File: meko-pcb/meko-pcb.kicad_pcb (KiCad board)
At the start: 4 copper layers, 37 x 69 mm, 213 parts, among them IC2 TPS7A2033PDBVR, IC4 TAD5212IRGER, IC5 AS5600-ASOM, J1 USB_C_Receptacle_USB2.0_16P, J3 GDEY0154D67, J4 Conn_ARM_SWD_TagConnect_TC203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, J5 503398-1892, Q1 SS8050, Q2 Si1308EDL, SW1 SW_Push, SW2 SW_Push, SW3 SW_Push, SW4 SW_Push, SW5 SW_Push, SW6 SW_Push, SW7 SW_Push, SW9 SW_Push, U2 nRF5340-QKxx, U3 nPM1300-CAXX, Y1 32MHz, Y2 32.768 kHz

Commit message: started layout
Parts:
- removed U3: nPM1300-CAXX, PCM_nordic-lib-kicad-npm:BGA-35_7x5_3.077x2.3775mm
- added U1: nPM1300-QEXX, Package_DFN_QFN:QFN-32-1EP_5x5mm_P0.5mm_EP3.6x3.6mm_ThermalVias, B.Cu at (104.0, 78.5)
- AE1, C13, C18, C31, C32, C7, C8, D1, D10, D12, D14, D6, D7, D8, D9, JP4, L1, L2, L5, U2, Y1, Y2: moved to B.Cu
- R10, R11, R12, R13, R14, R15, R16, R17, R18, R19, R2, R3, R4, R5, R6, R7, R8, R9: footprint Resistor_SMD:R_0402_1005Metric -> Resistor_SMD:R_0603_1608Metric
- moved C13 80.6 mm to (108.7, 61.1), turned to 180 degrees
- moved C18 79.7 mm to (107.0, 64.6), turned to 90 degrees
- moved C7 79.4 mm to (103.0, 66.8), turned to 180 degrees
- moved C8 77.1 mm to (100.7, 69.5), turned to 90 degrees
- moved C53 76.1 mm to (106.4, 54.4), turned to -90 degrees
- moved C54 72.9 mm to (99.6, 50.2), turned to -90 degrees
- moved D14 72.5 mm to (89.4, 16.1), turned to 90 degrees
- moved D12 71.8 mm to (92.4, 16.1), turned to 90 degrees
- moved C51 71.6 mm to (104.6, 57.6), turned to 90 degrees
- moved D6 71.6 mm to (104.2, 16.1), turned to 90 degrees
- moved D10 71.4 mm to (95.3, 16.1), turned to 90 degrees
- moved D7 71.3 mm to (101.2, 16.1), turned to 90 degrees
- moved D9 71.2 mm to (98.3, 16.1), turned to 90 degrees
- moved C63 66.5 mm to (104.6, 54.5), turned to -90 degrees
- moved C49 63.2 mm to (96.0, 53.2)
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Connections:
- net Net-(U2-AIN6/P0.27) renamed /PMIC_GPIO4
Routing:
- net /DISPL_VCOM: track 0.00 -> 4.10 mm

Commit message: almost finished with general layout
this will most certanily evolve
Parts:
- added C39: 1uF, Capacitor_SMD:C_0603_1608Metric, F.Cu at (100.5, 71.4)
- added TP7: DISPL_SDA, TestPoint:TestPoint_Pad_D1.0mm, F.Cu at (120.1, 71.9)
- C1, C11, C12, C17, C19, C2, C22, C30, C35, C37, C42, C44, L3, R10, R12, R6, R9: moved to B.Cu
- D8: moved to F.Cu
- L1: value 10uH -> 2.2nH; footprint Inductor_SMD:L_1008_2520Metric -> Inductor_SMD:L_0603_1608Metric
- moved C35 83.1 mm to (99.3, 37.3), turned to 180 degrees
- moved C22 78.2 mm to (104.5, 69.5)
- moved C34 77.5 mm to (94.3, 37.5)
- moved C15 76.3 mm to (104.3, 64.7)
- moved C30 75.9 mm to (94.7, 33.1)
- moved C1 75.7 mm to (99.8, 60.8), turned to 90 degrees
- moved C12 73.7 mm to (100.2, 76.7), turned to -90 degrees
- moved C24 72.2 mm to (104.3, 66.3)
- moved C2 72.0 mm to (96.2, 60.8), turned to 90 degrees
- moved C11 70.6 mm to (93.8, 74.6), turned to -90 degrees
- moved C17 70.4 mm to (98.5, 76.7), turned to -90 degrees
- moved C5 70.3 mm to (94.3, 75.2), turned to 180 degrees
- moved C9 70.2 mm to (94.3, 76.9), turned to 180 degrees
- moved C14 69.9 mm to (97.5, 75.2)
- moved C20 69.5 mm to (97.5, 76.9)
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
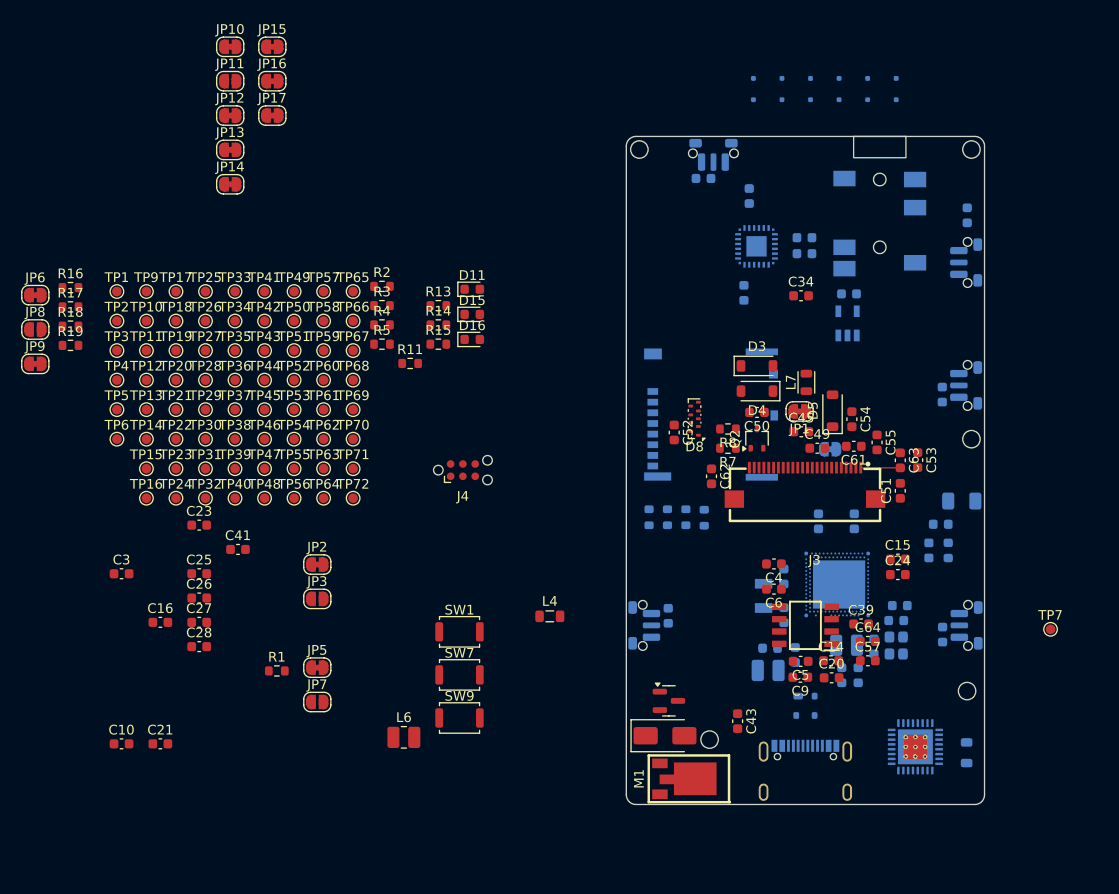
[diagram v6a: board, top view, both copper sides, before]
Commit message: finished first pass of rough layout
i still need to add 3d modles
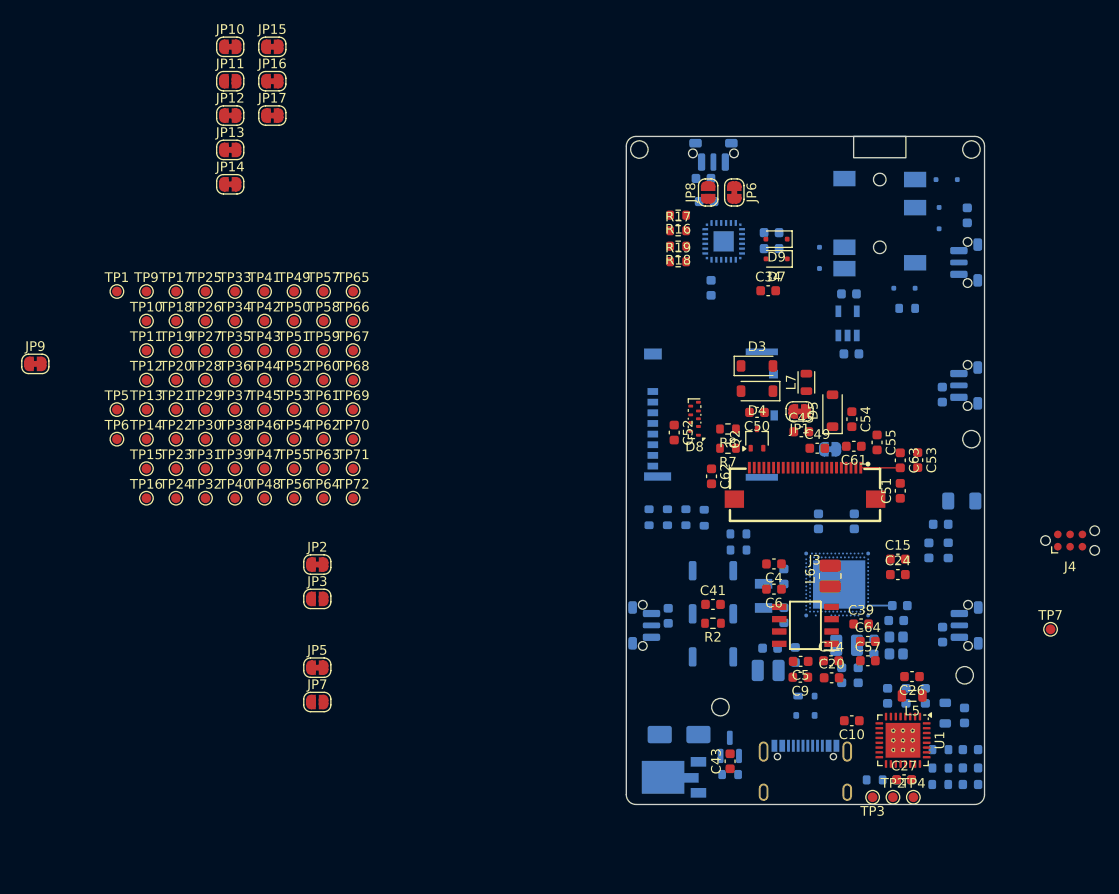
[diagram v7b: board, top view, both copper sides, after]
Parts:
- C16, C21, C23, C25, C28, C3, D11, D15, D16, D2, L4, M1, Q1, R1, R11, R13, R14, R15, R3, R4, R5, SW1, SW7, SW9: moved to B.Cu
- D7, D9, L5, U1: moved to F.Cu
- moved TP2 94.0 mm to (103.8, 89.2)
- moved TP4 92.9 mm to (106.0, 89.3)
- moved TP3 90.7 mm to (101.7, 89.2), turned to 180 degrees
- moved C3 83.6 mm to (105.0, 87.4)
- moved C25 80.4 mm to (111.2, 80.8), turned to 90 degrees
- moved C16 77.4 mm to (105.2, 78.8), turned to 90 degrees
- moved C23 77.0 mm to (107.2, 78.8), turned to 90 degrees
- moved C10 75.5 mm to (99.6, 81.3), turned to 180 degrees
- moved C21 75.3 mm to (103.3, 78.8), turned to 90 degrees
- moved C27 74.6 mm to (105.0, 87.4)
- moved C26 74.1 mm to (105.8, 76.8), turned to 180 degrees
- moved C28 73.8 mm to (99.5, 43.5), turned to 180 degrees
- moved JP6 73.0 mm to (87.5, 26.8), turned to -90 degrees
- moved JP8 70.9 mm to (84.8, 26.8), turned to 90 degrees
- moved R14 70.3 mm to (108.7, 87.9)
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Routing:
- net +3V3: track 0.00 -> 2.50 mm

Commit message: moved some stuff around
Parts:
- moved C18 3.33 mm to (107.0, 67.0)
- moved L1 3.33 mm to (109.0, 67.0)
- moved C13 3.33 mm to (108.2, 64.3)
- moved AE1 3.33 mm to (110.4, 61.9)
- moved D2 1.67 mm to (80.1, 82.8)
- moved C4 0.99 mm to (91.8, 64.2)
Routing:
- net /XC2: track 0.00 -> 6.39 mm
- net /XC1: track 0.00 -> 5.87 mm
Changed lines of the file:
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@@
 	(footprint "Capacitor_SMD:C_0603_1608Metric"
 		(layer "F.Cu")
-		(at 91.55 65.1525 180)
+		(at 91.845 64.2125 180)
 		(descr "Capacitor SMD 0603 (1608 Metric), square (rectangular) end terminal, IPC-7351 nominal, (Body size source: IPC-SM-782 page 76, https://www.pcb-3d.com/wordpress/wp-content/uploads/ipc-sm-782a_amendment_1_and_2.pdf), generated with kicad-footprint-generator")
 		(tags "capacitor")
@@
 	(footprint "PJ-242:AUDIO-SMD_PJ-342"
 		(layer "B.Cu")
-		(at 102.48 29.99625 180)
+		(at 102.48 29.99375 180)
 		(property "Reference" "CN2"
 			(at 0 10.102 0)
@@
 	(footprint "Inductor_SMD:L_0603_1608Metric"
 		(layer "B.Cu")
-		(at 109.55 63.7525 90)
+		(at 109.02206 67.036651 90)
 		(descr "Inductor SMD 0603 (1608 Metric), square (rectangular) end terminal, IPC-7351 nominal, (Body size source: http://www.tortai-tech.com/upload/download/2011102023233369053.pdf), generated with kicad-footprint-generator")
 		(tags "inductor")
@@
 	(footprint "Diode_SMD:D_1206_3216Metric"
 		(layer "B.Cu")
-		(at 110.95 58.6525 180)
+		(at 110.42206 61.936651 180)
 		(descr "Diode SMD 1206 (3216 Metric), square (rectangular) end terminal, IPC-7351 nominal, (Body size source: http://www.tortai-tech.com/upload/download/2011102023233369053.pdf), generated with kicad-footprint-generator")
 		(tags "diode")
@@
 	(footprint "Capacitor_SMD:C_0603_1608Metric"
 		(layer "B.Cu")
-		(at 108.775 61.0525 180)
+		(at 108.24706 64.336651 180)
 		(descr "Capacitor SMD 0603 (1608 Metric), square (rectangular) end terminal, IPC-7351 nominal, (Body size source: IPC-SM-782 page 76, https://www.pcb-3d.com/wordpress/wp-content/uploads/ipc-sm-782a_amendment_1_and_2.pdf), generated with kicad-footprint-generator")
 		(tags "capacitor")
@@
 	(footprint "Diode_SMD:D_SMA"
 		(layer "B.Cu")
-		(at 81.751339 82.772893)
+		(at 80.08 82.7525)
 		(descr "Diode SMA (DO-214AC)")
 		(tags "Diode SMA (DO-214AC)")
@@
 	(footprint "Capacitor_SMD:C_0603_1608Metric"
 		(layer "B.Cu")
-		(at 107.55 63.7525 90)
+		(at 107.02206 67.036651 90)
 		(descr "Capacitor SMD 0603 (1608 Metric), square (rectangular) end terminal, IPC-7351 nominal, (Body size source: IPC-SM-782 page 76, https://www.pcb-3d.com/wordpress/wp-content/uploads/ipc-sm-782a_amendment_1_and_2.pdf), generated with kicad-footprint-generator")
 		(tags "capacitor")
@@
 	)
 	(segment
+		(start 101.3 69.4525)
+		(end 101.28 69.4725)
+		(width 0.2)
+		(layer "B.Cu")
+		(net 6)
+	)
+	(segment
 		(start 103.775 69.4525)
 		(end 101.3 69.4525)
@@
 	)
 	(segment
-		(start 101.3 69.4525)
-		(end 101.28 69.4725)
+		(start 104.88 72.6975)
+		(end 104.88 71.07075)
 		(width 0.2)
 		(layer "B.Cu")
-		(net 6)
+		(net 33)
+	)
+	(segment
+		(start 104.07775 70.1185)
+		(end 101.526 70.1185)
+		(width 0.2)
+		(layer "B.Cu")
+		(net 33)
+	)
+	(segment
+		(start 101.526 70.1185)
+		(end 101.28 69.8725)
+		(width 0.2)
+		(layer "B.Cu")
+		(net 33)
+	)
+	(segment
+		(start 104.955 70.99575)
+		(end 104.07775 70.1185)
+		(width 0.2)
+		(layer "B.Cu")
+		(net 33)
+	)
+	(segment
+		(start 104.88 71.07075)
+		(end 104.955 70.99575)
+		(width 0.2)
+		(layer "B.Cu")
+		(net 33)
+	)
+	(segment
+		(start 101.214 73.7815)
+		(end 101.88 74.4475)
+		(width 0.2)
+		(layer "B.Cu")
+		(net 34)
+	)
+	(segment
+		(start 101.214 72.775904)
+		(end 101.214 73.7815)
+		(width 0.2)
+		(layer "B.Cu")
+		(net 34)
+	)
+	(segment
+		(start 100.88 72.441904)
+		(end 101.214 72.775904)
+		(width 0.2)
+		(layer "B.Cu")
+		(net 34)
+	)
+	(segment
+		(start 101.88 74.4475)
+		(end 103.48 74.4475)
+		(width 0.2)
+		(layer "B.Cu")
+		(net 34)
+	)
+	(segment
+		(start 100.88 70.0725)
+		(end 100.88 72.441904)
+		(width 0.2)
+		(layer "B.Cu")
+		(net 34)
 	)
 	(segment
@@
 	)
 	(segment
-		(start 109.5375 64.5275)
-		(end 109.55 64.54)
+		(start 109.00956 67.811651)
+		(end 109.02206 67.824151)
 		(width 0.2)
 		(layer "B.Cu")
